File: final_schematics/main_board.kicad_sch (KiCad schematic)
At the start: 6 parts, among them J1 Input device 1, J2 Input device 1, J5 Barrel_Jack, U1 PCA9685PW, U2 PCA9685PW

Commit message: Test code on main board
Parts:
- added M1: Motor_DC, symbol Motor:Motor_DC
- added Q1: PN2222A, Package_TO_SOT_THT:TO-92_Inline, symbol Transistor_BJT:PN2222A
- added R1: 330, symbol Device:R_Small
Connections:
- net GND: now also Q1.1 (E)
- net at A1.16 (D13): now also R1.1
- new net: Q1.2 (B), R1.2
- new net: M1.2 (-), Q1.3 (C)
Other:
- moved on the sheet: J5, U1, U2

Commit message: Almost ready to play a full game
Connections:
- net +5V: now also M1.1 (+)
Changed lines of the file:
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@@
+	(wire
+		(pts
+			(xy 113.03 97.79) (xy 114.3 97.79)
+		)
+		(stroke
+			(width 0)
+			(type default)
+		)
+	)
 	(wire
 		(pts

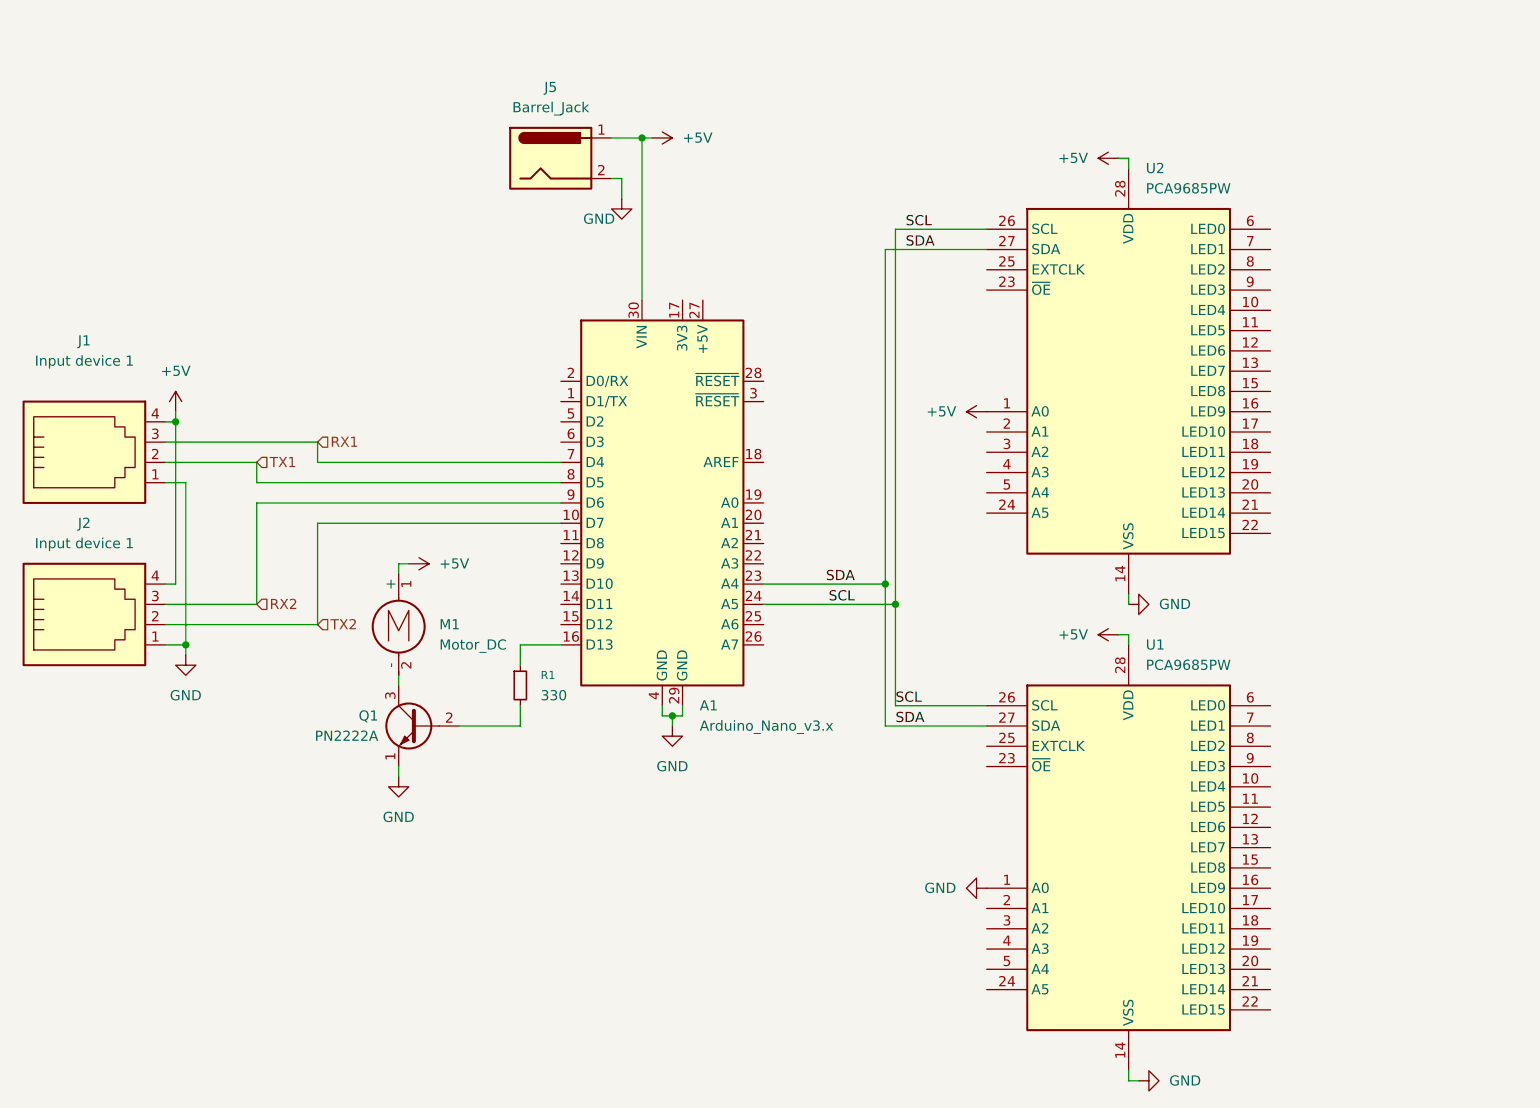
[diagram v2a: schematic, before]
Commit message: Add flowcharts
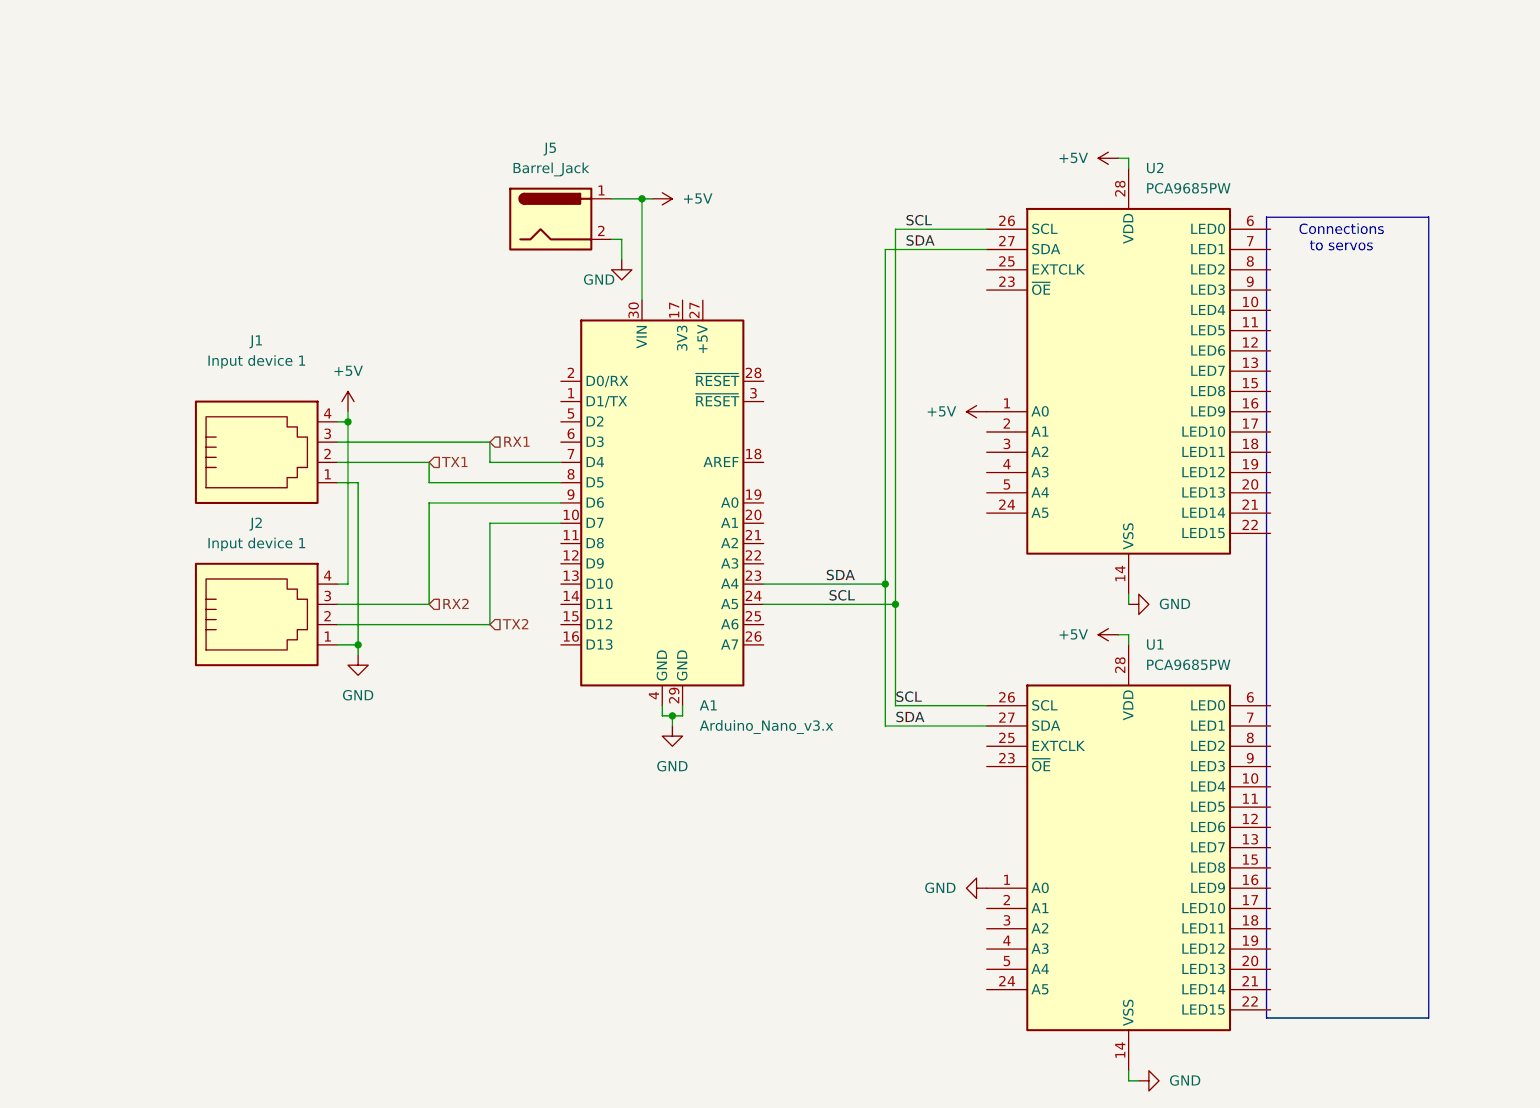
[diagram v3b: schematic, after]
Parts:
- removed M1: Motor_DC, symbol Motor:Motor_DC
- removed Q1: PN2222A, Package_TO_SOT_THT:TO-92_Inline, symbol Transistor_BJT:PN2222A
- removed R1: 330, symbol Device:R_Small
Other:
- note added: "Connections to servos"
- moved on the sheet: J1, J2, J5
